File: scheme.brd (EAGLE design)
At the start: 100 x 80 mm, 36 parts, among them J1 22-05-7048-04, J2 22-05-7028-02

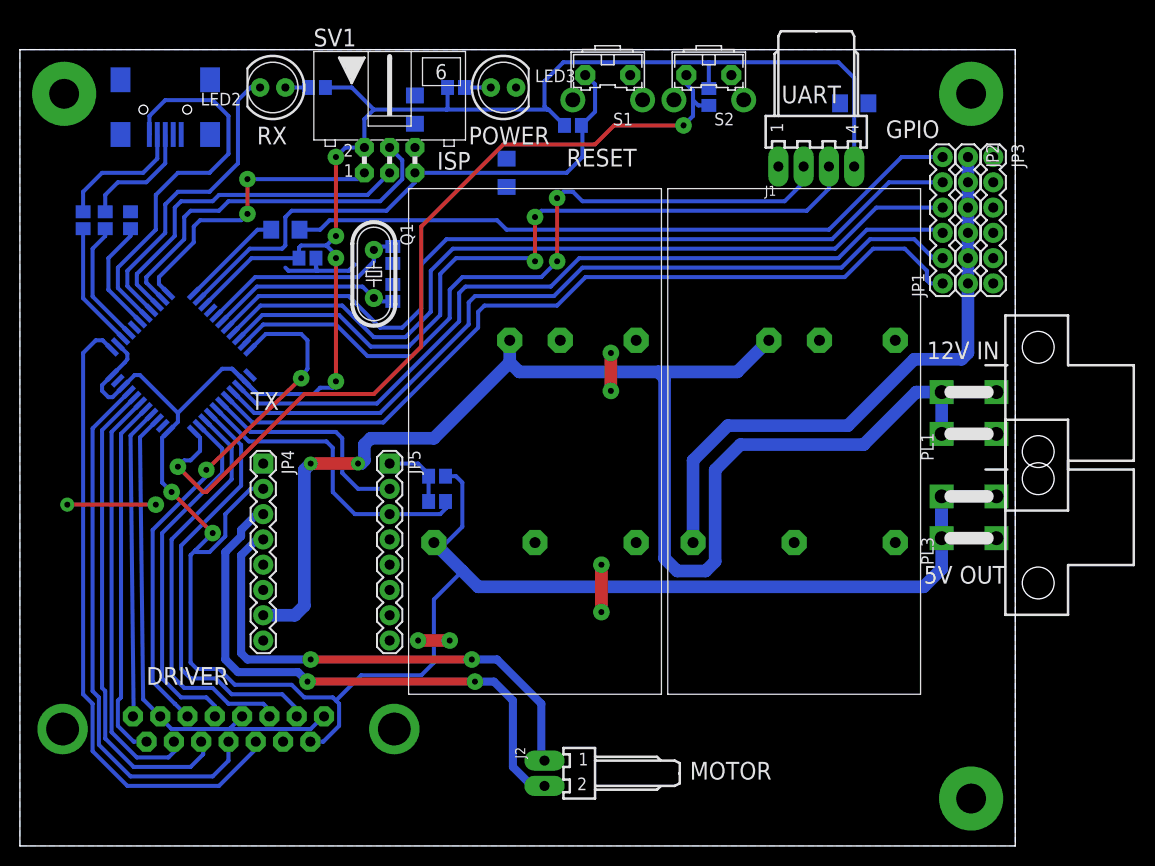
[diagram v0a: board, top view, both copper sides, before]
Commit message: Reroute HWB button
Signed-off-by: Nikita 'webconn' Maslov <wkernelteam@gmail.com>
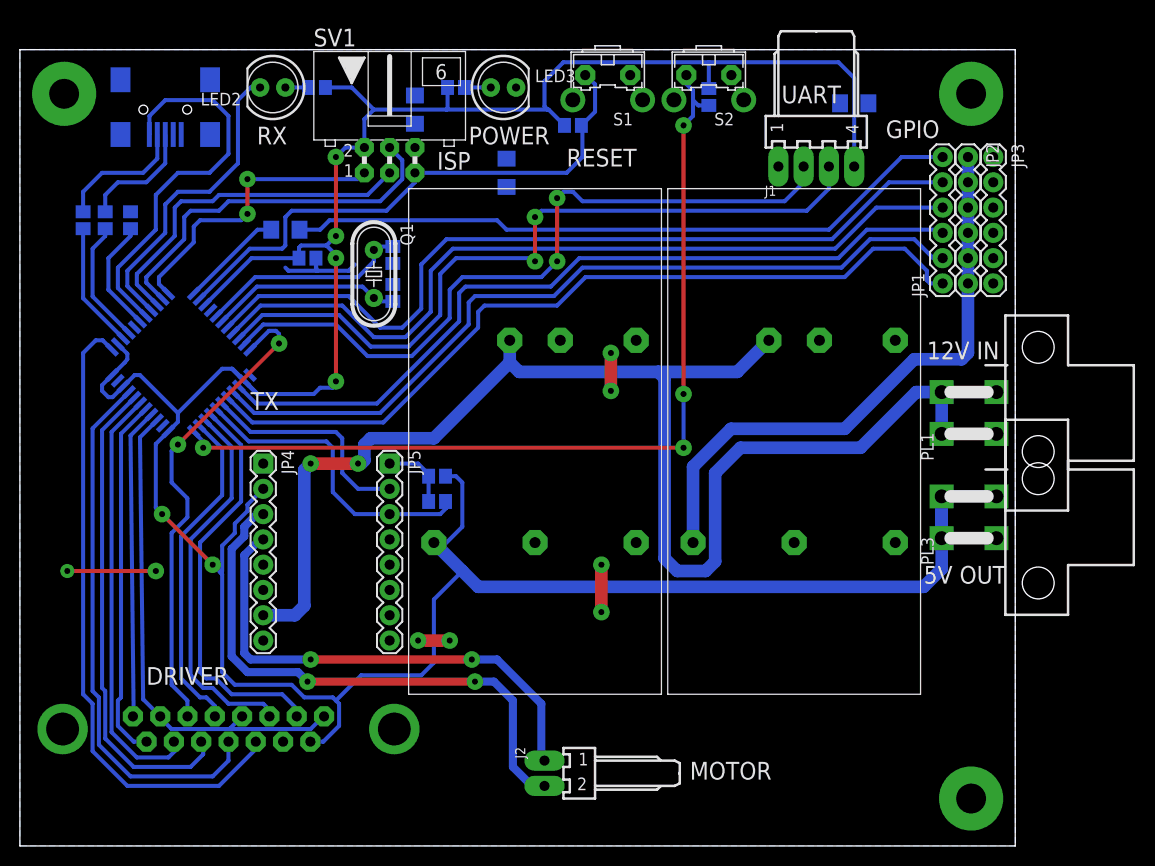
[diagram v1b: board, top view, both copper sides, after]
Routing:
- net HWB: track 86.8 -> 90.6 mm, vias 2 -> 4
- net RELAY: track 52.4 -> 48.7 mm
- net VCC: track 319.1 -> 315.9 mm
- net Z_DIR: track 41.2 -> 38.5 mm
- net X_DIR: track 36.3 -> 33.6 mm
- net Z_STEP: track 43.4 -> 40.9 mm
- net M1: track 57.8 -> 56.7 mm
- net M2: track 50.8 -> 50.2 mm

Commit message: Add extra capacitors and rework silk
Signed-off-by: Nikita 'webconn' Maslov <wkernelteam@gmail.com>
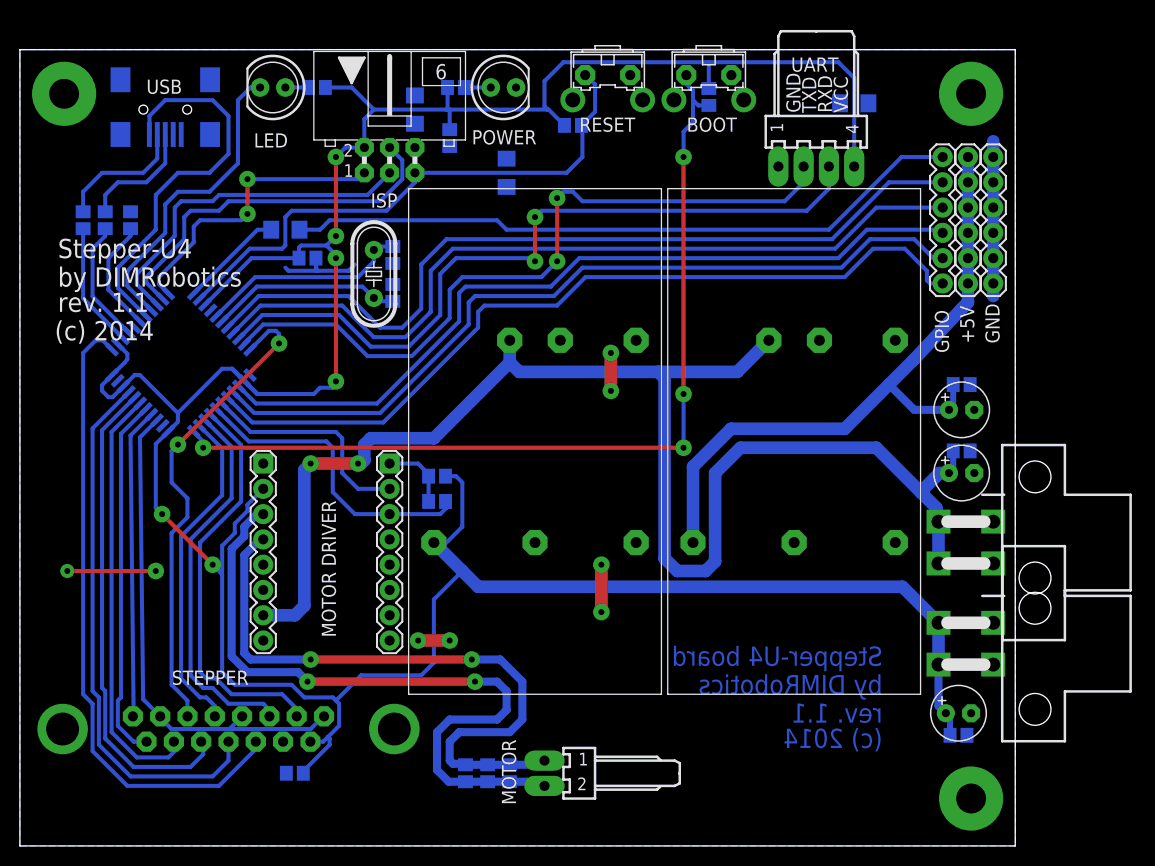
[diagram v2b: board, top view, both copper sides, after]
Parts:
- added C10, C11, C12, C13, C14, C15, C5, C6: 100n, resistor:C0805
- added C7, C8, C9: (no value), rcl:E2,5-6
- moved PL1 13.0 mm to (97.8, 30.5)
- moved PL3 12.7 mm to (97.8, 20.3)
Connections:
- net +12V: now also C10.2, C8.+
- net +5V: now also C11.2, C9.+
- net GND: now also C10.1, C11.1, C12.1, C5.1, C6.1, C7.-, C8.-, C9.-
- net M1: now also C13.2, C14.2, C15.2
- net M2: now also C13.1, C14.1, C15.1
- net VCC: now also C12.2, C5.2, C6.2, C7.+
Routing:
- net M2: track 50.2 -> 65.8 mm
- net GND: track 29.9 -> 45.4 mm
- net M1: track 56.7 -> 70.1 mm
- net VCC: track 315.9 -> 323.4 mm
- net +5V: track 59.7 -> 67.2 mm
- net +12V: track 138.4 -> 145.6 mm
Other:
- board text added: "(c) 2014"
- board text added: "+5V"
- board text added: "BOOT"
- board text added: "GND"
- board text added: "LED"
- board text added: "MOTOR DRIVER"
- board text added: "RXD"
- board text added: "STEPPER"
- board text added: "Stepper-U4"
- board text added: "Stepper-U4 board"
- board text added: "TXD"
- board text added: "USB"
- board text added: "VCC"
- board text added: "by DIMRobotics"
- board text added: "rev. 1.1"
- board text removed: "12V IN"
- board text removed: "5V OUT"
- board text removed: "DRIVER"
- board text removed: "RX"
- board text removed: "TX"

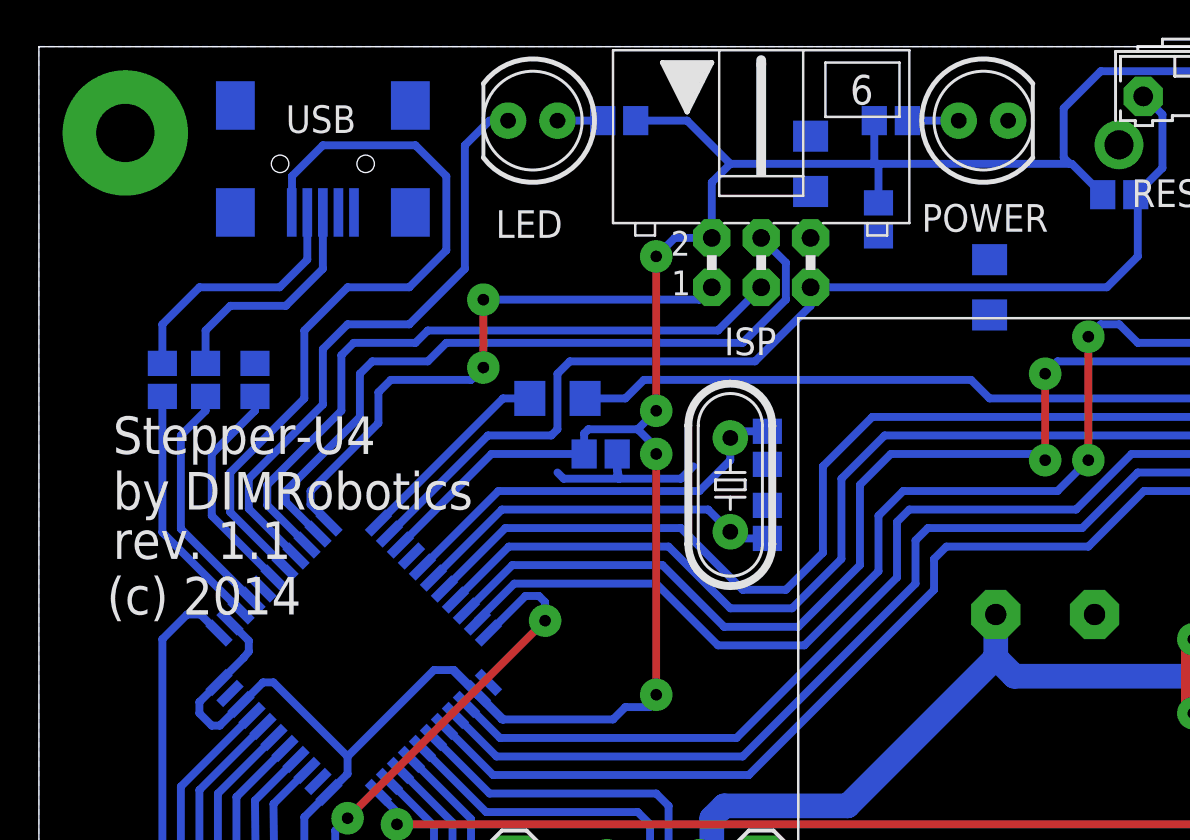
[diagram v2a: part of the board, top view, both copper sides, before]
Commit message: Add USB power jumper
Signed-off-by: Nikita 'webconn' Maslov <wkernelteam@gmail.com>
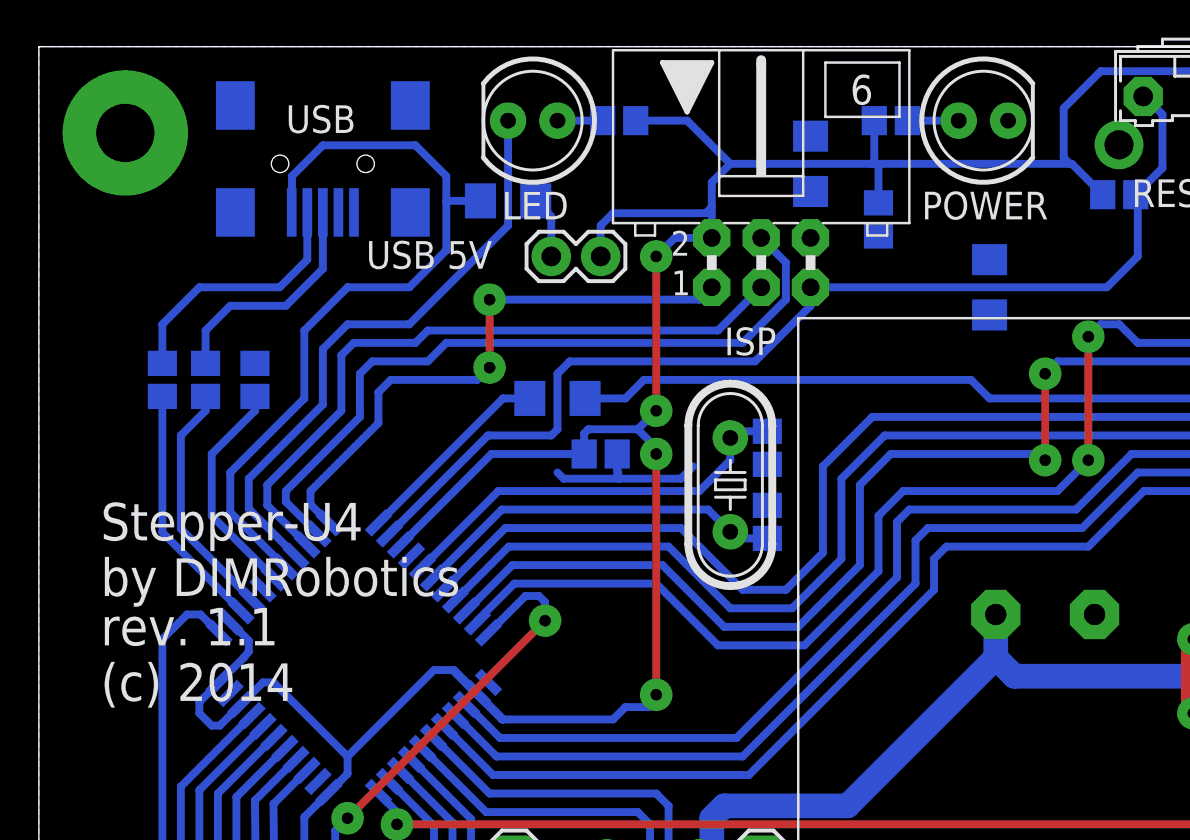
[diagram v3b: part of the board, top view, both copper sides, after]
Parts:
- added JP6: M02PTH, SparkFun-Connectors:1X02
- added R13: 0, rcl:R1206
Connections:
- new net N$12: JP6.1, R13.1
- net N$11: now also R13.2
- net VCC: now also JP6.2
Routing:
- net VCC: track 323.4 -> 331.1 mm
- net N$12: track 0.00 -> 3.19 mm
- net N$11: track 38.8 -> 40.6 mm
- net LED: track 31.3 -> 30.8 mm
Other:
- board text added: "USB 5V"
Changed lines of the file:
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@@
 <text x="31.75" y="20.955" size="1.4224" layer="25" font="vector" ratio="14" rot="R90">MOTOR DRIVER</text>
 <text x="12.7" y="75.565" size="1.4224" layer="25" font="vector" ratio="14">USB</text>
-<text x="23.495" y="70.1675" size="1.4224" layer="25" font="vector" ratio="14">LED</text>
-<text x="45.4025" y="70.485" size="1.4224" layer="25" font="vector" ratio="14">POWER</text>
+<text x="23.8125" y="71.12" size="1.4224" layer="25" font="vector" ratio="14">LED</text>
+<text x="45.4025" y="71.12" size="1.4224" layer="25" font="vector" ratio="14">POWER</text>
 <text x="35.2425" y="64.135" size="1.4224" layer="25" font="vector" ratio="14">ISP</text>
 <text x="77.47" y="77.7875" size="1.4224" layer="25" font="vector" ratio="14">UART</text>
@@
 <text x="78.4225" y="73.66" size="1.4224" layer="25" font="vector" ratio="14" rot="R90">GND</text>
 <text x="83.185" y="73.66" size="1.4224" layer="25" font="vector" ratio="14" rot="R90">VCC</text>
-<text x="3.81" y="59.055" size="1.9304" layer="25" font="vector" ratio="14">Stepper-U4</text>
-<text x="3.81" y="56.1975" size="1.9304" layer="25" font="vector" ratio="14">by DIMRobotics</text>
-<text x="3.81" y="53.6575" size="1.9304" layer="25" font="vector" ratio="14">rev. 1.1</text>
-<text x="3.4925" y="50.8" size="1.9304" layer="25" font="vector" ratio="14">(c) 2014</text>
+<text x="3.175" y="54.61" size="1.9304" layer="25" font="vector" ratio="14">Stepper-U4</text>
+<text x="3.175" y="51.7525" size="1.9304" layer="25" font="vector" ratio="14">by DIMRobotics</text>
+<text x="3.175" y="49.2125" size="1.9304" layer="25" font="vector" ratio="14">rev. 1.1</text>
+<text x="3.175" y="46.355" size="1.9304" layer="25" font="vector" ratio="14">(c) 2014</text>
+<text x="16.8275" y="68.58" size="1.4224" layer="25" font="vector" ratio="14">USB 5V</text>
 </plain>
 <attributes>
@@
 <element name="C14" library="resistor" package="C0805" value="100n" x="46.99" y="7.3025" smashed="yes" rot="MR270"/>
 <element name="C15" library="resistor" package="C0805" value="100n" x="44.7675" y="7.3025" smashed="yes" rot="MR270"/>
+<element name="JP6" library="SparkFun-Connectors" package="1X02" value="M02PTH" x="26.3525" y="69.215" smashed="yes"/>
+<element name="R13" library="rcl" package="R1206" value="0" x="24.13" y="72.0725" rot="MR0"/>
 </elements>
 <signals>
@@
 <contactref element="R6" pad="2"/>
 <contactref element="SV1" pad="2"/>
-<wire x1="34.6075" y1="70.1675" x2="34.6075" y2="73.025" width="0.4064" layer="16"/>
+<wire x1="34.6075" y1="70.1675" x2="34.6075" y2="71.755" width="0.4064" layer="16"/>
+<wire x1="34.6075" y1="71.755" x2="34.6075" y2="73.025" width="0.4064" layer="16"/>
 <wire x1="34.6075" y1="73.025" x2="35.56" y2="73.9775" width="0.4064" layer="16"/>
 <wire x1="30.695" y1="76.2" x2="33.3375" y2="76.2" width="0.4064" layer="16"/>
@@
 <wire x1="93.4475" y1="11.1125" x2="93.4475" y2="12.915" width="0.6096" layer="16"/>
 <wire x1="93.4475" y1="12.915" x2="93.0275" y2="13.335" width="0.6096" layer="16"/>
+<contactref element="JP6" pad="2"/>
+<wire x1="28.8925" y1="69.215" x2="28.8925" y2="70.8025" width="0.4064" layer="16"/>
+<wire x1="28.8925" y1="70.8025" x2="29.5275" y2="71.4375" width="0.4064" layer="16"/>
+<wire x1="29.5275" y1="71.4375" x2="34.29" y2="71.4375" width="0.4064" layer="16"/>
+<wire x1="34.29" y1="71.4375" x2="34.6075" y2="71.755" width="0.4064" layer="16"/>
 </signal>
 <signal name="N$4">
@@
 <wire x1="14.605" y1="74.93" x2="19.3675" y2="74.93" width="0.4064" layer="16"/>
 <wire x1="19.3675" y1="74.93" x2="20.955" y2="73.3425" width="0.4064" layer="16"/>
-<wire x1="20.955" y1="73.3425" x2="20.955" y2="69.5325" width="0.4064" layer="16"/>
+<wire x1="20.955" y1="73.3425" x2="20.955" y2="72.0725" width="0.4064" layer="16"/>
+<wire x1="20.955" y1="72.0725" x2="20.955" y2="69.5325" width="0.4064" layer="16"/>
 <wire x1="20.955" y1="69.5325" x2="19.05" y2="67.6275" width="0.4064" layer="16"/>
 <wire x1="19.05" y1="67.6275" x2="15.875" y2="67.6275" width="0.4064" layer="16"/>
@@
 <wire x1="9.8425" y1="58.1025" x2="9.8425" y2="56.058871875" width="0.4064" layer="16"/>
 <wire x1="9.8425" y1="56.058871875" x2="12.65696875" y2="53.244403125" width="0.4064" layer="16"/>
+<contactref element="R13" pad="2"/>
+<wire x1="22.708" y1="72.0725" x2="20.955" y2="72.0725" width="0.4064" layer="16"/>
 </signal>
 <signal name="MOSI">
@@
 <contactref element="U$1" pad="11"/>
 <contactref element="SV1" pad="1"/>
-<via x="22.86" y="63.5" extent="1-16" drill="0.6" diameter="1.6764" shape="octagon"/>
-<wire x1="22.86" y1="63.5" x2="22.86" y2="66.9925" width="0.4064" layer="1"/>
-<via x="22.86" y="66.9925" extent="1-16" drill="0.6" diameter="1.6764" shape="octagon"/>
-<wire x1="22.225" y1="62.865" x2="22.86" y2="63.5" width="0.4064" layer="16"/>
+<via x="23.1775" y="63.5" extent="1-16" drill="0.6" diameter="1.6764" shape="octagon"/>
+<wire x1="23.1775" y1="63.5" x2="23.1775" y2="66.9925" width="0.4064" layer="1"/>
+<via x="23.1775" y="66.9925" extent="1-16" drill="0.6" diameter="1.6764" shape="octagon"/>
+<wire x1="22.5425" y1="62.865" x2="23.1775" y2="63.5" width="0.4064" layer="16"/>
 <wire x1="14.919709375" y1="55.50714375" x2="13.97" y2="56.456853125" width="0.4064" layer="16"/>
 <wire x1="13.97" y1="56.456853125" x2="13.97" y2="57.15" width="0.4064" layer="16"/>
@@
 <wire x1="17.4625" y1="60.6425" x2="17.4625" y2="62.23" width="0.4064" layer="16"/>
 <wire x1="17.4625" y1="62.23" x2="18.0975" y2="62.865" width="0.4064" layer="16"/>
-<wire x1="18.0975" y1="62.865" x2="22.225" y2="62.865" width="0.4064" layer="16"/>
-<wire x1="22.86" y1="66.9925" x2="33.9725" y2="66.9925" width="0.4064" layer="16"/>
+<wire x1="18.0975" y1="62.865" x2="22.5425" y2="62.865" width="0.4064" layer="16"/>
+<wire x1="23.1775" y1="66.9925" x2="33.9725" y2="66.9925" width="0.4064" layer="16"/>
 <wire x1="33.9725" y1="66.9925" x2="34.6075" y2="67.6275" width="0.4064" layer="16"/>
 </signal>
@@
 <wire x1="14.605" y1="64.4525" x2="15.875" y2="65.7225" width="0.4064" layer="16"/>
 <wire x1="15.875" y1="65.7225" x2="19.05" y2="65.7225" width="0.4064" layer="16"/>
-<wire x1="19.05" y1="65.7225" x2="21.9075" y2="68.58" width="0.4064" layer="16"/>
-<wire x1="21.9075" y1="68.58" x2="21.9075" y2="74.93" width="0.4064" layer="16"/>
-<wire x1="21.9075" y1="74.93" x2="23.1775" y2="76.2" width="0.4064" layer="16"/>
-<wire x1="23.1775" y1="76.2" x2="24.13" y2="76.2" width="0.4064" layer="16"/>
+<wire x1="19.05" y1="65.7225" x2="24.13" y2="70.8025" width="0.4064" layer="16"/>
+<wire x1="24.13" y1="70.8025" x2="24.13" y2="76.2" width="0.4064" layer="16"/>
+</signal>
+<signal name="N$12">
+<contactref element="JP6" pad="1"/>
+<contactref element="R13" pad="1"/>
+<wire x1="26.3525" y1="69.215" x2="26.3525" y2="71.272" width="0.4064" layer="16"/>
+<wire x1="26.3525" y1="71.272" x2="25.552" y2="72.0725" width="0.4064" layer="16"/>
 </signal>
 </signals>
